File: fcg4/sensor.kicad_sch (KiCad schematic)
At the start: 1 part, among them U2 ICM-42688-P

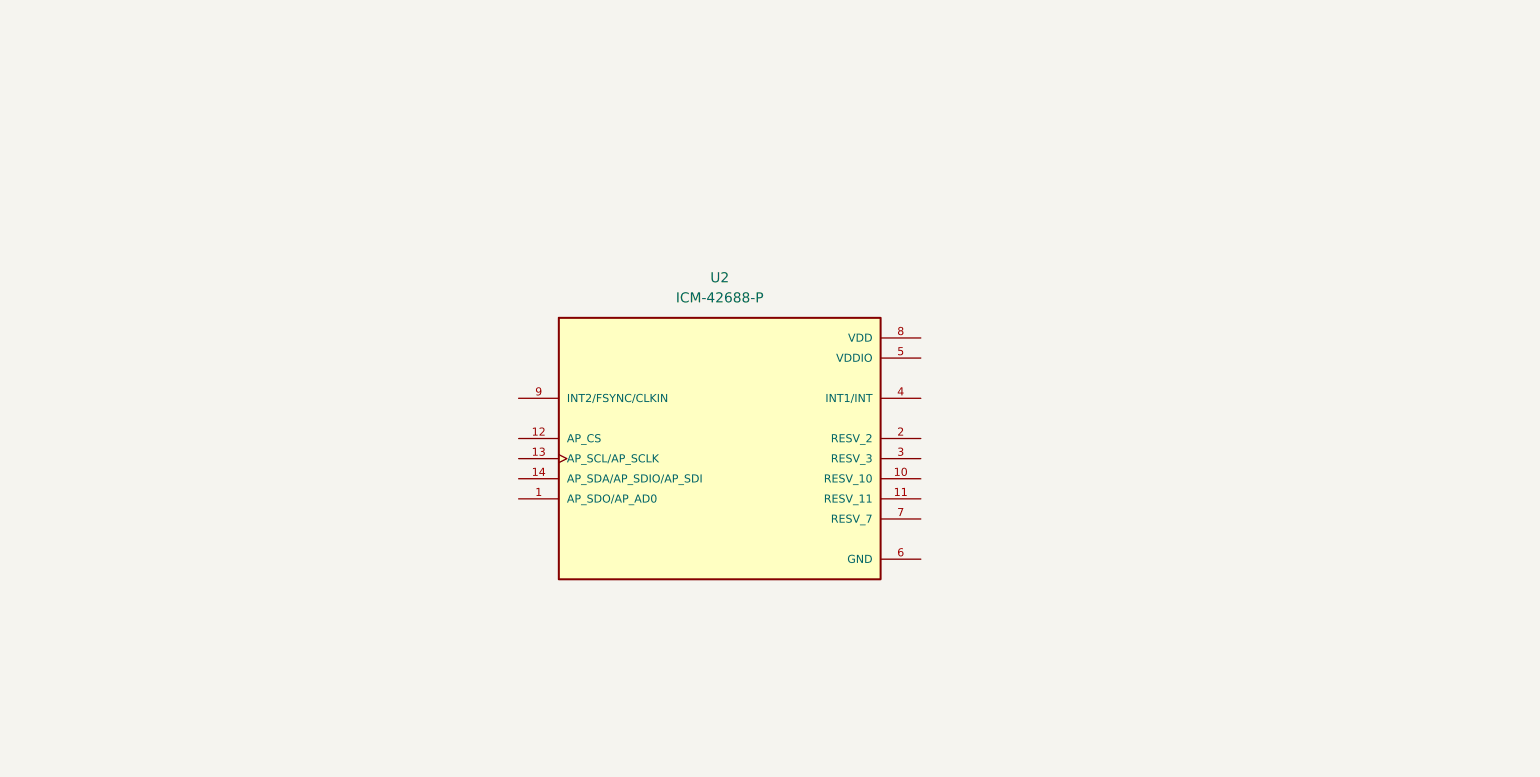
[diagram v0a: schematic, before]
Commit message: add first few components
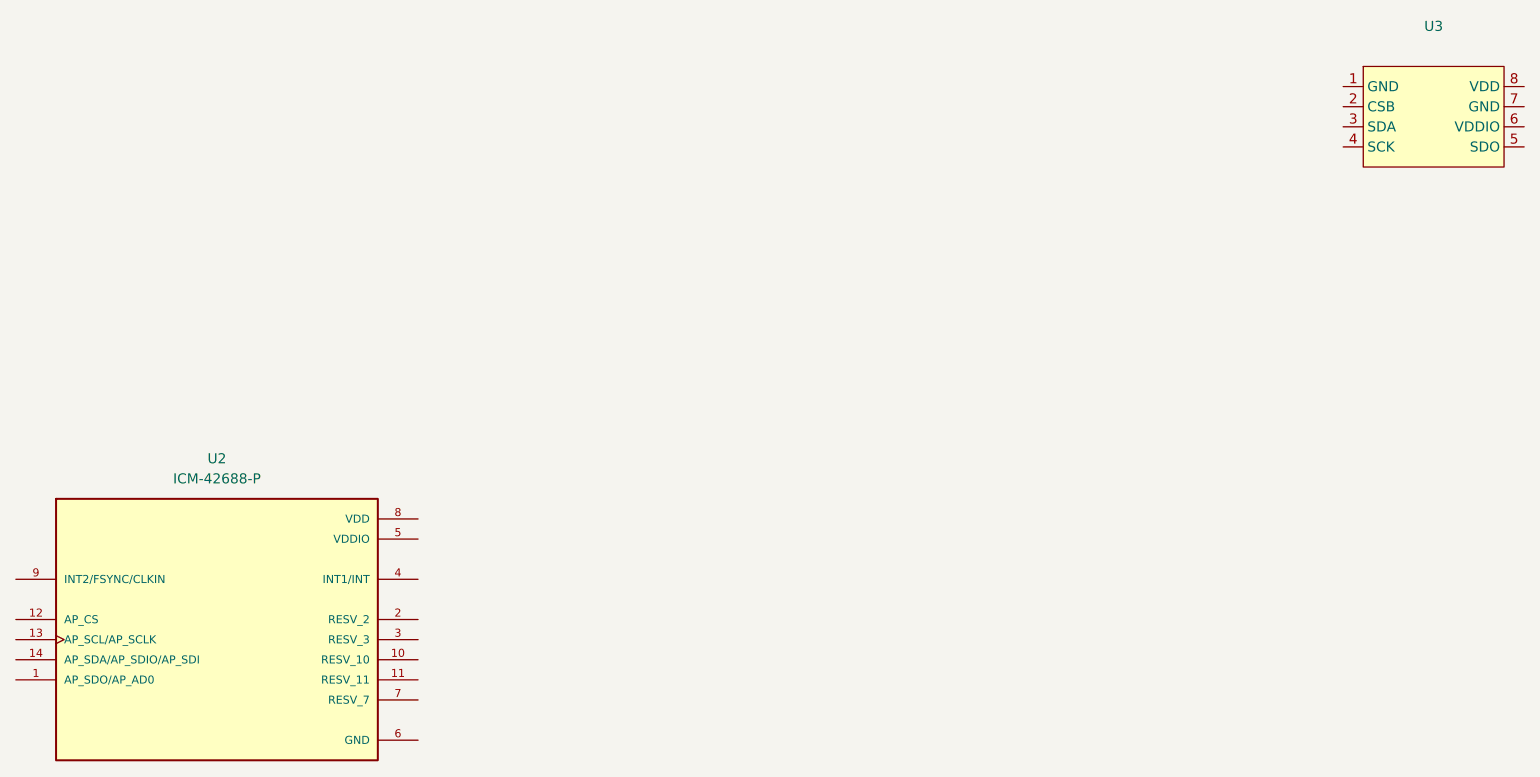
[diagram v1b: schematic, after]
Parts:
- added U3: ~, ProLib_pcs_2026-02-12:SENSOR-SMD_SPL06-001, symbol fcg4:SPL06-001
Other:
- moved on the sheet: U2
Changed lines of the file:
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@@
 	(symbol
 		(lib_id "fcg4:ICM-42688-P")
-		(at 132.08 93.98 0)
+		(at 68.58 116.84 0)
 		(unit 1)
 		(exclude_from_sim no)
@@
 		(fields_autoplaced yes)
 		(property "Reference" "U2"
-			(at 132.08 73.66 0)
+			(at 68.58 96.52 0)
 			(effects
 				(font
@@
 		)
 		(property "Value" "ICM-42688-P"
-			(at 132.08 76.2 0)
+			(at 68.58 99.06 0)
 			(effects
 				(font
@@
 		)
 		(property "Footprint" "fcg4_fp:PQFN50P300X250X97-14N"
-			(at 131.572 125.984 0)
+			(at 68.072 148.844 0)
 			(effects
 				(font
@@
 		)
 		(property "Datasheet" ""
-			(at 132.08 93.98 0)
+			(at 68.58 116.84 0)
 			(effects
 				(font
@@
 		)
 		(property "Description" ""
-			(at 132.08 93.98 0)
+			(at 68.58 116.84 0)
 			(effects
 				(font
@@
 		)
 		(property "DigiKey_Part_Number" "1428-ICM-42688-PCT-ND"
-			(at 132.08 75.438 0)
+			(at 68.58 98.298 0)
 			(effects
 				(font
@@
 		)
 		(property "SnapEDA_Link" "https://www.snapeda.com/parts/ICM-42688-P/TDK+InvenSense/view-part/?ref=snap"
-			(at 133.604 64.008 0)
+			(at 70.104 86.868 0)
 			(effects
 				(font
@@
 		)
 		(property "MAXIMUM_PACKAGE_HEIGHT" "0.97mm"
-			(at 132.334 59.436 0)
+			(at 68.834 82.296 0)
 			(effects
 				(font
@@
 		)
 		(property "Package" "LGA-14 TDK InvenSense"
-			(at 132.334 73.152 0)
+			(at 68.834 96.012 0)
 			(effects
 				(font
@@
 		)
 		(property "Check_prices" "https://www.snapeda.com/parts/ICM-42688-P/TDK+InvenSense/view-part/?ref=eda"
-			(at 132.334 70.104 0)
+			(at 68.834 92.964 0)
 			(effects
 				(font
@@
 		)
 		(property "STANDARD" "IPC-7351B"
-			(at 133.35 130.556 0)
+			(at 69.85 153.416 0)
 			(effects
 				(font
@@
 		)
 		(property "PARTREV" "1.2"
-			(at 132.842 52.578 0)
+			(at 69.342 75.438 0)
 			(effects
 				(font
@@
 		)
 		(property "MF" "TDK InvenSense"
-			(at 133.858 56.388 0)
+			(at 70.358 79.248 0)
 			(effects
 				(font
@@
 		)
 		(property "MP" "ICM-42688-P"
-			(at 132.08 121.666 0)
+			(at 68.58 144.526 0)
 			(effects
 				(font
@@
 		)
 		(property "Description_1" "Accelerometer, Gyroscope, 6 Axis Sensor - Output"
-			(at 132.842 118.364 0)
+			(at 69.342 141.224 0)
 			(effects
 				(font
@@
 		)
 		(property "MANUFACTURER" "TDK InvenSense"
-			(at 133.35 61.468 0)
+			(at 69.85 84.328 0)
 			(effects
 				(font
@@
 					(unit 1)
 				)
+			)
+		)
+	)
+	(symbol
+		(lib_id "fcg4:SPL06-001")
+		(at 222.25 53.34 0)
+		(unit 1)
+		(exclude_from_sim no)
+		(in_bom yes)
+		(on_board yes)
+		(dnp no)
+		(fields_autoplaced yes)
+		(property "Reference" "U3"
+			(at 222.25 41.91 0)
+			(effects
+				(font
+					(size 1.27 1.27)
+				)
+			)
+		)
+		(property "Value" "~"
+			(at 222.25 44.45 0)
+			(effects
+				(font
+					(size 1.27 1.27)
+				)
+			)
+		)
+		(property "Footprint" "ProLib_pcs_2026-02-12:SENSOR-SMD_SPL06-001"
+			(at 222.25 42.164 0)
+			(effects
+				(font
+					(size 1.27 1.27)
+				)
+				(hide yes)
+			)
+		)
+		(property "Datasheet" "https://item.szlcsc.com/datasheet/SPL06-001/2782076.html"
+			(at 222.25 62.484 0)
+			(effects
+				(font
+					(size 1.27 1.27)
+				)
+				(hide yes)
+			)
+		)
+		(property "Description" "Pressure range:30Kpa~1.1bar Pressure range:30Kpa~1.1bar Voltage - Supply:1.7V~3.6V Voltage - Supply:1.7V~3.6V Standby Current:1uA Interface:I2C；SPI Operating Temperature:-40°C~+85°C Operating Temperature:-40°C~+85°C Absolute Accuracy:1hpa Relative Accuracy:0."
+			(at 223.774 70.866 0)
+			(effects
+				(font
+					(size 1.27 1.27)
+				)
+				(hide yes)
+			)
+		)
+		(property "Manufacturer Part" "SPL06-001"
+			(at 222.25 68.326 0)
+			(effects
+				(font
+					(size 1.27 1.27)
+				)
+				(hide yes)
+			)
+		)
+		(property "Manufacturer" "Goertek(歌尔)"
+			(at 222.504 74.422 0)
+			(effects
+				(font
+					(size 1.27 1.27)
+				)
+				(hide yes)
+			)
+		)
+		(property "Supplier Part" "C2684428"
+			(at 222.25 61.214 0)
+			(effects
+				(font
+					(size 1.27 1.27)
+				)
+				(hide yes)
+			)
+		)
+		(property "Supplier" "LCSC"
+			(at 221.996 45.974 0)
+			(effects
+				(font
+					(size 1.27 1.27)
+				)
+				(hide yes)
+			)
+		)
+		(property "LCSC Part Name" "普通气压传感器 停产"
+			(at 222.25 65.532 0)
+			(effects
+				(font
+					(size 1.27 1.27)
+				)
+				(hide yes)
+			)
+		)
+		(pin "1"
+		)
+		(pin "8"
+		)
+		(pin "3"
+		)
+		(pin "2"
+		)
+		(pin "4"
+		)
+		(pin "7"
+		)
+		(pin "5"
+		)
+		(pin "6"
+		)
+		(instances
+			(project ""
+				(path "/ebe93c2f-0aae-4f69-99fc-930f63b0ac94/4b9bfb89-4b08-43bb-8e52-e82396130844"
+					(reference "U3")
+					(unit 1)
+				)
